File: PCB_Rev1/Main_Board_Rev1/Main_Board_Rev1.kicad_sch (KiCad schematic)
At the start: 2 parts, among them J1 PRT-14017

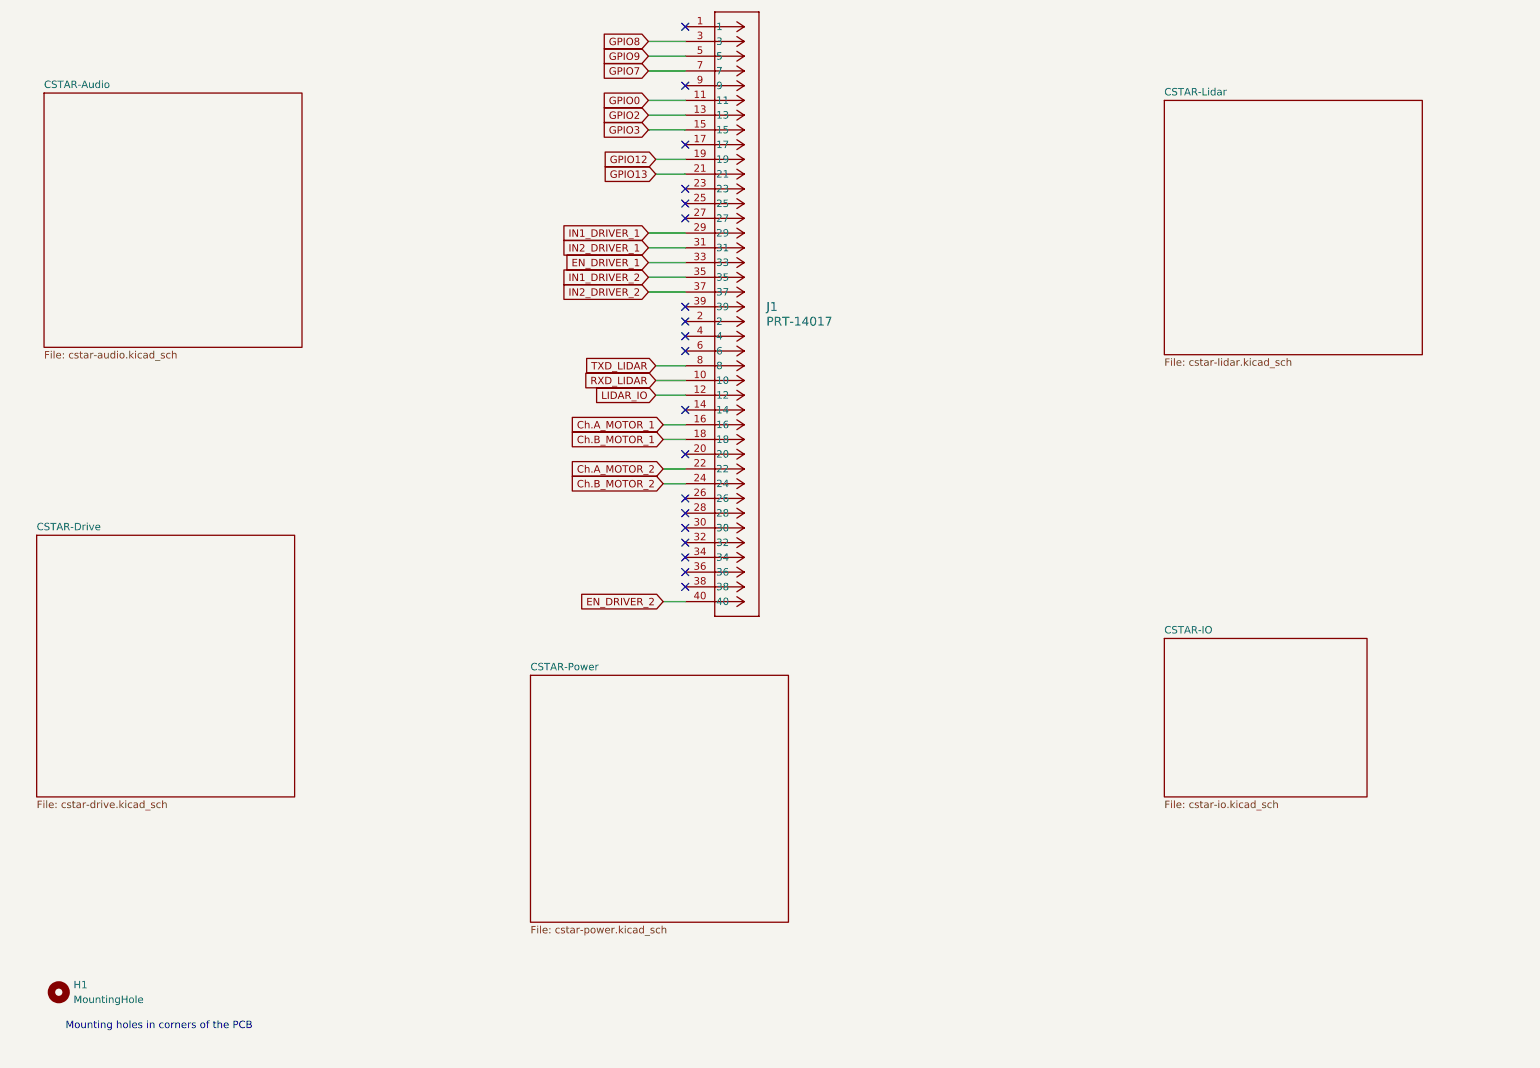
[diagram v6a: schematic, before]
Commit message: Multiple Mounting Holes Added + GPIO Connections Added for RGB
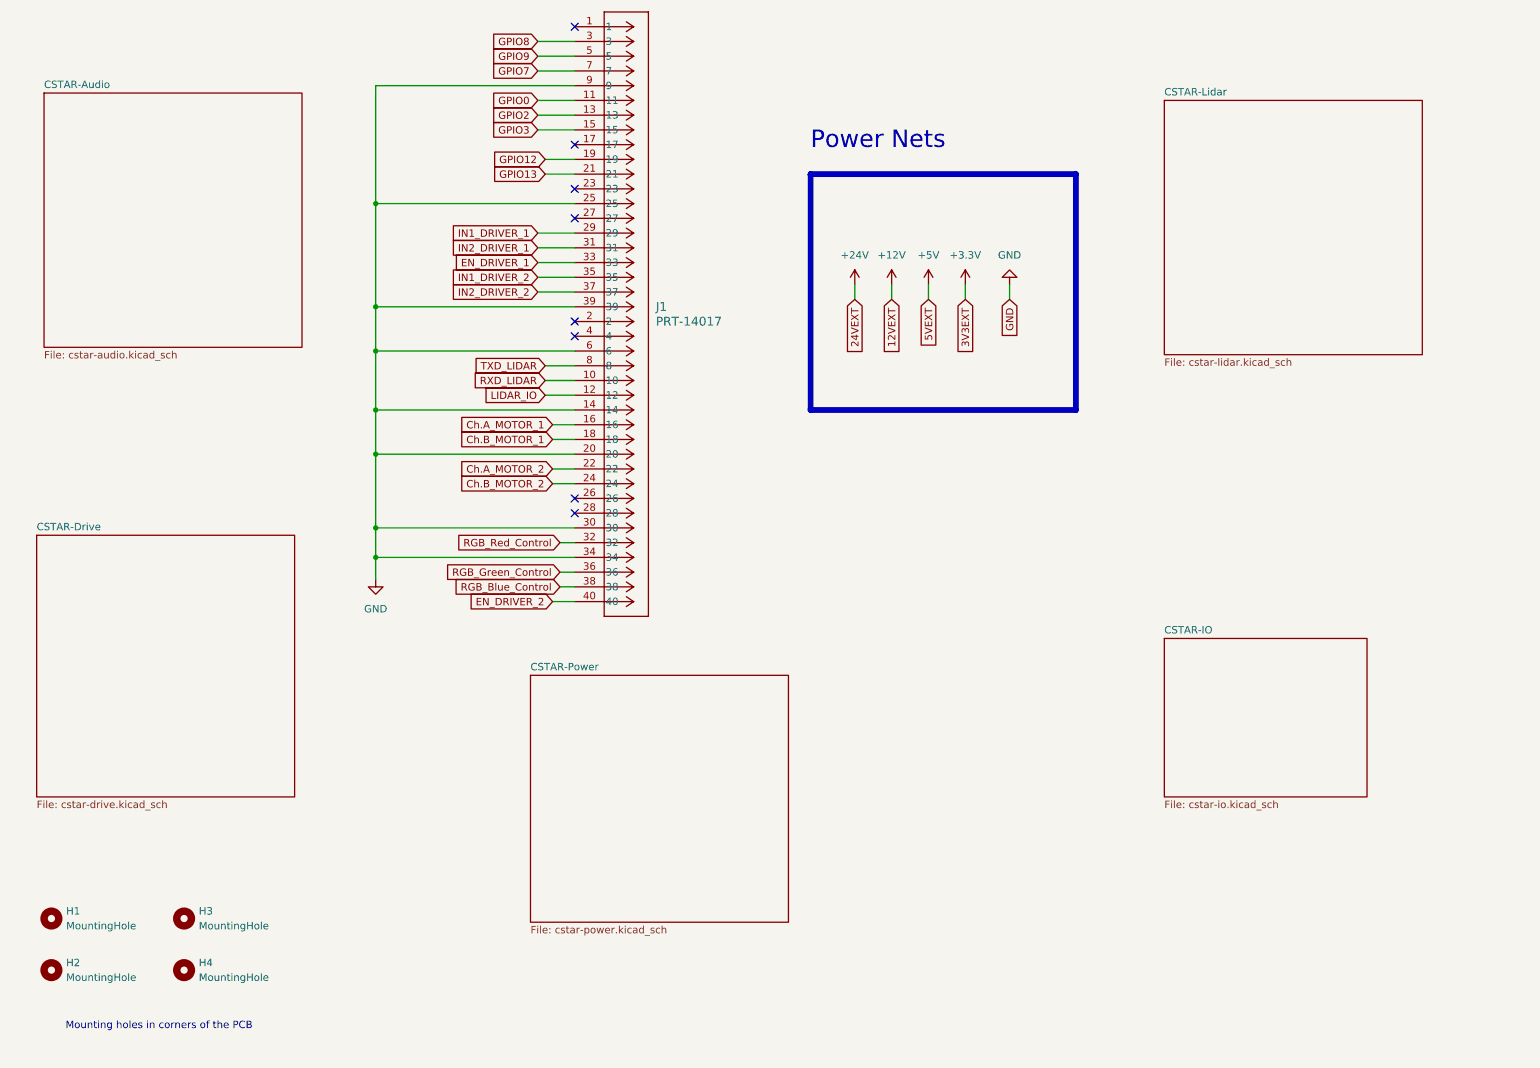
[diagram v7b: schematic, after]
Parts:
- added H2, H3, H4: MountingHole, MountingHole:MountingHole_5.3mm_M5, symbol Mechanical:MountingHole
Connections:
- net GND: now reaches J1.14
- net GND: now also J1.20, J1.25, J1.30, J1.34, J1.39, J1.6, J1.9
- net RGB_Red_Control: now reaches J1.32
- net RGB_Green_Control: now reaches J1.36
- net RGB_Blue_Control: now reaches J1.38
- no-connect marks 19 -> 8
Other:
- note added: "Power Nets"
- moved on the sheet: H1, J1

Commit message: mounting holes set
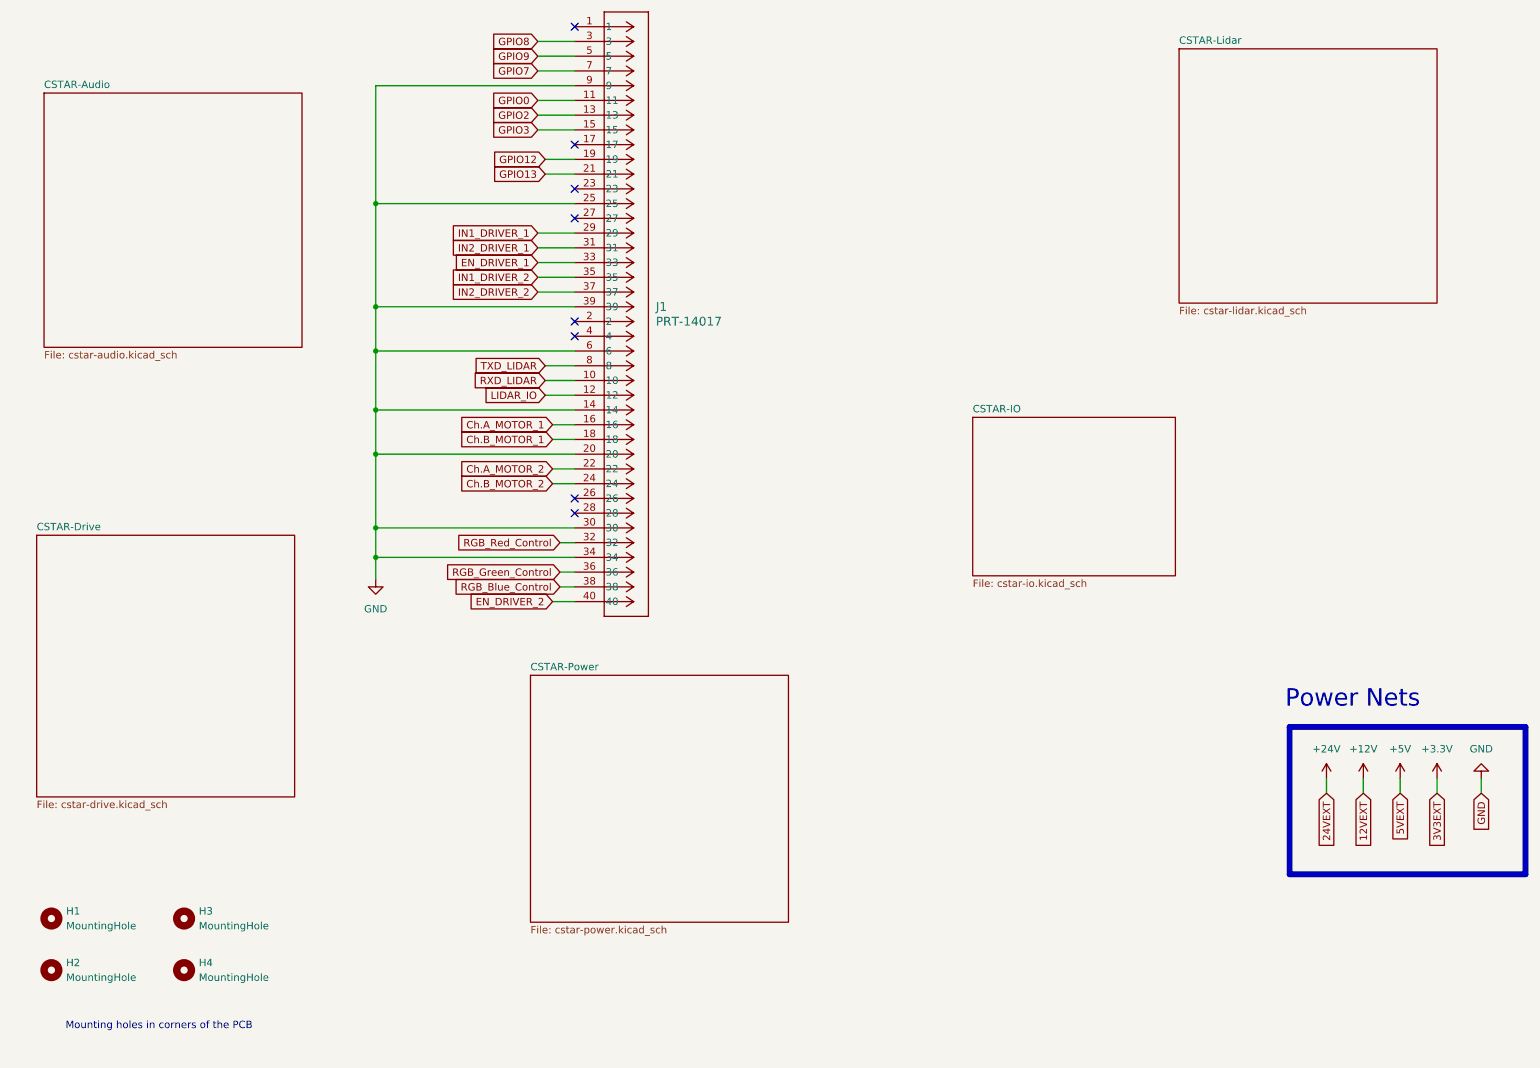
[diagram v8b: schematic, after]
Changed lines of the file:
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@@
 	(wire
 		(pts
-			(xy 162.56 62.23) (xy 162.56 64.77)
+			(xy 243.84 147.32) (xy 243.84 149.86)
 		)
 		(stroke
@@
 	(wire
 		(pts
-			(xy 168.91 62.23) (xy 168.91 64.77)
-		)
-		(stroke
-			(width 0)
-			(type default)
-		)
-	)
-	(wire
-		(pts
-			(xy 181.61 62.23) (xy 181.61 64.77)
+			(xy 250.19 147.32) (xy 250.19 149.86)
+		)
+		(stroke
+			(width 0)
+			(type default)
+		)
+	)
+	(wire
+		(pts
+			(xy 262.89 147.32) (xy 262.89 149.86)
 		)
 		(stroke
@@
 	(wire
 		(pts
-			(xy 189.23 62.23) (xy 189.23 64.77)
+			(xy 270.51 147.32) (xy 270.51 149.86)
 		)
 		(stroke
@@
 	(wire
 		(pts
-			(xy 175.26 62.23) (xy 175.26 64.77)
+			(xy 256.54 147.32) (xy 256.54 149.86)
 		)
 		(stroke
@@
 	)
 	(rectangle
-		(start 154.94 43.18)
-		(end 200.66 83.82)
+		(start 237.49 138.43)
+		(end 278.13 163.83)
 		(stroke
 			(width 1)
@@
 	(text "Power Nets"
 		(exclude_from_sim no)
-		(at 154.94 39.116 0)
+		(at 236.728 135.382 0)
 		(effects
 			(font
@@
 	(global_label "3V3EXT"
 		(shape input)
-		(at 181.61 64.77 270)
-		(fields_autoplaced yes)
-		(effects
-			(font
-				(size 1.27 1.27)
-			)
-			(justify right)
-		)
-		(property "Intersheetrefs" "${INTERSHEET_REFS}"
-			(at 181.61 74.5889 90)
+		(at 262.89 149.86 270)
+		(fields_autoplaced yes)
+		(effects
+			(font
+				(size 1.27 1.27)
+			)
+			(justify right)
+		)
+		(property "Intersheetrefs" "${INTERSHEET_REFS}"
+			(at 262.89 159.6789 90)
 			(effects
 				(font
@@
 	(global_label "12VEXT"
 		(shape input)
-		(at 168.91 64.77 270)
-		(fields_autoplaced yes)
-		(effects
-			(font
-				(size 1.27 1.27)
-			)
-			(justify right)
-		)
-		(property "Intersheetrefs" "${INTERSHEET_REFS}"
-			(at 168.91 74.5889 90)
+		(at 250.19 149.86 270)
+		(fields_autoplaced yes)
+		(effects
+			(font
+				(size 1.27 1.27)
+			)
+			(justify right)
+		)
+		(property "Intersheetrefs" "${INTERSHEET_REFS}"
+			(at 250.19 159.6789 90)
 			(effects
 				(font
@@
 	(global_label "5VEXT"
 		(shape input)
-		(at 175.26 64.77 270)
-		(fields_autoplaced yes)
-		(effects
-			(font
-				(size 1.27 1.27)
-			)
-			(justify right)
-		)
-		(property "Intersheetrefs" "${INTERSHEET_REFS}"
-			(at 175.26 73.3794 90)
+		(at 256.54 149.86 270)
+		(fields_autoplaced yes)
+		(effects
+			(font
+				(size 1.27 1.27)
+			)
+			(justify right)
+		)
+		(property "Intersheetrefs" "${INTERSHEET_REFS}"
+			(at 256.54 158.4694 90)
 			(effects
 				(font
@@
 	(global_label "24VEXT"
 		(shape input)
-		(at 162.56 64.77 270)
-		(fields_autoplaced yes)
-		(effects
-			(font
-				(size 1.27 1.27)
-			)
-			(justify right)
-		)
-		(property "Intersheetrefs" "${INTERSHEET_REFS}"
-			(at 162.56 74.5889 90)
+		(at 243.84 149.86 270)
+		(fields_autoplaced yes)
+		(effects
+			(font
+				(size 1.27 1.27)
+			)
+			(justify right)
+		)
+		(property "Intersheetrefs" "${INTERSHEET_REFS}"
+			(at 243.84 159.6789 90)
 			(effects
 				(font
@@
 	(global_label "GND"
 		(shape input)
-		(at 189.23 64.77 270)
-		(fields_autoplaced yes)
-		(effects
-			(font
-				(size 1.27 1.27)
-			)
-			(justify right)
-		)
-		(property "Intersheetrefs" "${INTERSHEET_REFS}"
-			(at 189.23 71.6257 90)
+		(at 270.51 149.86 270)
+		(fields_autoplaced yes)
+		(effects
+			(font
+				(size 1.27 1.27)
+			)
+			(justify right)
+		)
+		(property "Intersheetrefs" "${INTERSHEET_REFS}"
+			(at 270.51 156.7157 90)
 			(effects
 				(font
@@
 	(symbol
 		(lib_id "power:+5V")
-		(at 162.56 62.23 0)
+		(at 243.84 147.32 0)
 		(unit 1)
 		(exclude_from_sim no)
@@
 		(fields_autoplaced yes)
 		(property "Reference" "#PWR058"
-			(at 162.56 66.04 0)
+			(at 243.84 151.13 0)
 			(effects
 				(font
@@
 		)
 		(property "Value" "+24V"
-			(at 162.56 57.15 0)
+			(at 243.84 142.24 0)
 			(effects
 				(font
@@
 		)
 		(property "Footprint" ""
-			(at 162.56 62.23 0)
+			(at 243.84 147.32 0)
 			(effects
 				(font
@@
 		)
 		(property "Datasheet" ""
-			(at 162.56 62.23 0)
+			(at 243.84 147.32 0)
 			(effects
 				(font
@@
 		)
 		(property "Description" "Power symbol creates a global label with name \"+5V\""
-			(at 162.56 62.23 0)
+			(at 243.84 147.32 0)
 			(effects
 				(font
@@
 	(symbol
 		(lib_id "power:GND")
-		(at 189.23 62.23 180)
+		(at 270.51 147.32 180)
 		(unit 1)
 		(exclude_from_sim no)
@@
 		(fields_autoplaced yes)
 		(property "Reference" "#PWR067"
-			(at 189.23 55.88 0)
+			(at 270.51 140.97 0)
 			(effects
 				(font
@@
 		)
 		(property "Value" "GND"
-			(at 189.23 57.15 0)
+			(at 270.51 142.24 0)
 			(effects
 				(font
@@
 		)
 		(property "Footprint" ""
-			(at 189.23 62.23 0)
+			(at 270.51 147.32 0)
 			(effects
 				(font
@@
 		)
 		(property "Datasheet" ""
-			(at 189.23 62.23 0)
+			(at 270.51 147.32 0)
 			(effects
 				(font
@@
 		)
 		(property "Description" "Power symbol creates a global label with name \"GND\" , ground"
-			(at 189.23 62.23 0)
+			(at 270.51 147.32 0)
 			(effects
 				(font
@@
 	(symbol
 		(lib_id "power:+5V")
-		(at 175.26 62.23 0)
+		(at 256.54 147.32 0)
 		(unit 1)
 		(exclude_from_sim no)
@@
 		(fields_autoplaced yes)
 		(property "Reference" "#PWR064"
-			(at 175.26 66.04 0)
+			(at 256.54 151.13 0)
 			(effects
 				(font
@@
 		)
 		(property "Value" "+5V"
-			(at 175.26 57.15 0)
+			(at 256.54 142.24 0)
 			(effects
 				(font
@@
 		)
 		(property "Footprint" ""
-			(at 175.26 62.23 0)
+			(at 256.54 147.32 0)
 			(effects
 				(font
@@
 		)
 		(property "Datasheet" ""
-			(at 175.26 62.23 0)
+			(at 256.54 147.32 0)
 			(effects
 				(font
@@
 		)
 		(property "Description" "Power symbol creates a global label with name \"+5V\""
-			(at 175.26 62.23 0)
+			(at 256.54 147.32 0)
 			(effects
 				(font
@@
 	(symbol
 		(lib_id "power:+3.3V")
-		(at 181.61 62.23 0)
+		(at 262.89 147.32 0)
 		(unit 1)
 		(exclude_from_sim no)
@@
 		(fields_autoplaced yes)
 		(property "Reference" "#PWR066"
-			(at 181.61 66.04 0)
+			(at 262.89 151.13 0)
 			(effects
 				(font
@@
 		)
 		(property "Value" "+3.3V"
-			(at 181.61 57.15 0)
+			(at 262.89 142.24 0)
 			(effects
 				(font
@@
 		)
 		(property "Footprint" ""
-			(at 181.61 62.23 0)
+			(at 262.89 147.32 0)
 			(effects
 				(font
@@
 		)
 		(property "Datasheet" ""
-			(at 181.61 62.23 0)
+			(at 262.89 147.32 0)
 			(effects
 				(font
@@
 		)
 		(property "Description" "Power symbol creates a global label with name \"+3.3V\""
-			(at 181.61 62.23 0)
+			(at 262.89 147.32 0)
 			(effects
 				(font
@@
 	(symbol
 		(lib_id "power:+5V")
-		(at 168.91 62.23 0)
+		(at 250.19 147.32 0)
 		(unit 1)
 		(exclude_from_sim no)
@@
 		(fields_autoplaced yes)
 		(property "Reference" "#PWR059"
-			(at 168.91 66.04 0)
+			(at 250.19 151.13 0)
 			(effects
 				(font
@@
 		)
 		(property "Value" "+12V"
-			(at 168.91 57.15 0)
+			(at 250.19 142.24 0)
 			(effects
 				(font
@@
 		)
 		(property "Footprint" ""
-			(at 168.91 62.23 0)
+			(at 250.19 147.32 0)
 			(effects
 				(font
@@
 		)
 		(property "Datasheet" ""
-			(at 168.91 62.23 0)
+			(at 250.19 147.32 0)
 			(effects
 				(font
@@
 		)
 		(property "Description" "Power symbol creates a global label with name \"+5V\""
-			(at 168.91 62.23 0)
+			(at 250.19 147.32 0)
 			(effects
 				(font
@@
 	)
 	(sheet
-		(at 215.9 30.48)
+		(at 218.44 21.59)
 		(size 44.45 43.815)
 		(fields_autoplaced yes)
@@
 		)
 		(property "Sheetname" "CSTAR-Lidar"
-			(at 215.9 29.7684 0)
+			(at 218.44 20.8784 0)
 			(effects
 				(font
@@
 		)
 		(property "Sheetfile" "cstar-lidar.kicad_sch"
-			(at 215.9 74.8796 0)
+			(at 218.44 65.9896 0)
 			(effects
 				(font
@@
 	)
 	(sheet
-		(at 215.9 123.19)
+		(at 182.88 85.09)
 		(size 34.925 27.305)
 		(fields_autoplaced yes)
@@
 		)
 		(property "Sheetname" "CSTAR-IO"
-			(at 215.9 122.4784 0)
+			(at 182.88 84.3784 0)
 			(effects
 				(font
@@
 		)
 		(property "Sheetfile" "cstar-io.kicad_sch"
-			(at 215.9 151.0796 0)
-			(effects
-				(font
+			(at 182.88 112.9796 0)
+			(effects
+				(font
